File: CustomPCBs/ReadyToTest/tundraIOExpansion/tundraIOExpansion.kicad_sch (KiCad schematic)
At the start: 58 parts, among them J1 Conn_01x25, J2 Conn_ARM_SWD_TagConnect_TC203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, J3 Conn_ARM_SWD_TagConnect_TC203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, U1 RP2040, U2 W25Q32JVSS, U4 W25Q32JVSS, U5 RP2040, Y1 12.000MHz, Y2 12.000MHz, Y3 32.768kHz

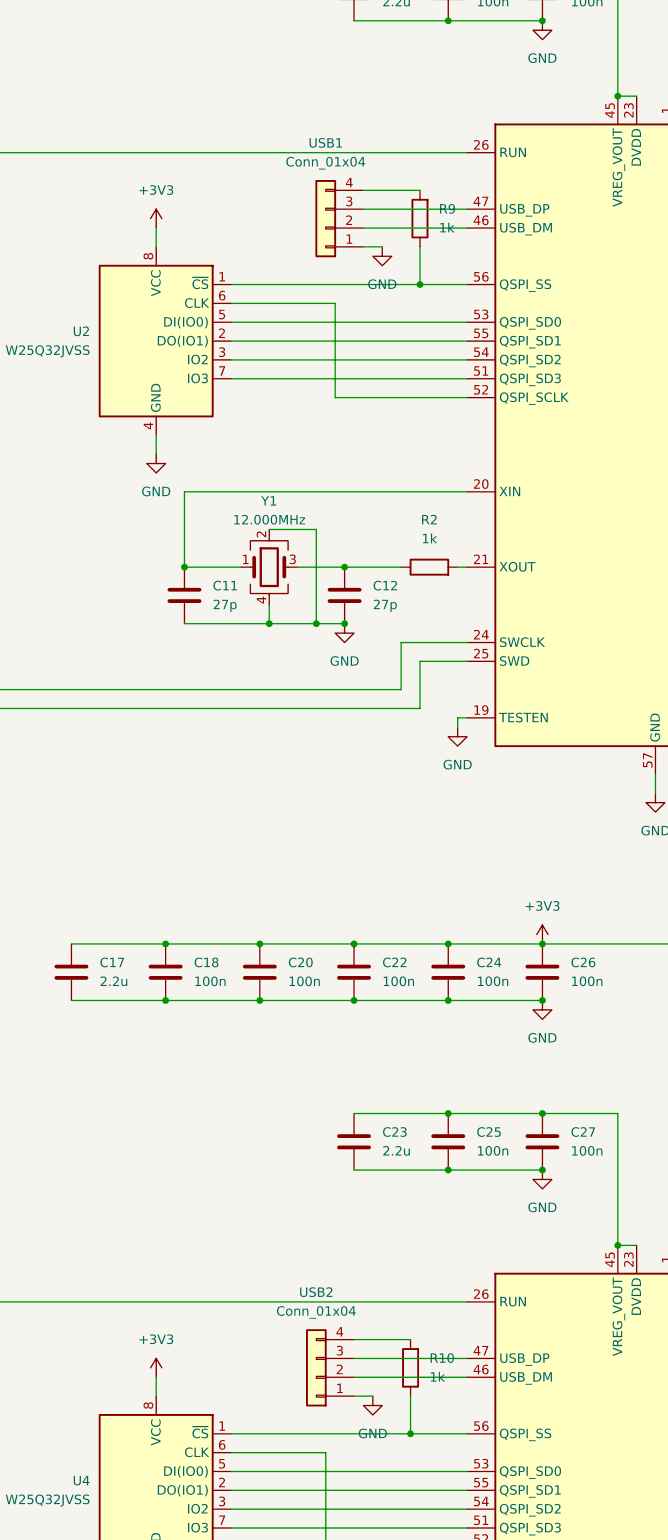
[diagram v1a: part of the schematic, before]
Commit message: Fixing USB connectors on main board
Forgot to invert the USB connectors, these were wrong too on the first
batch.
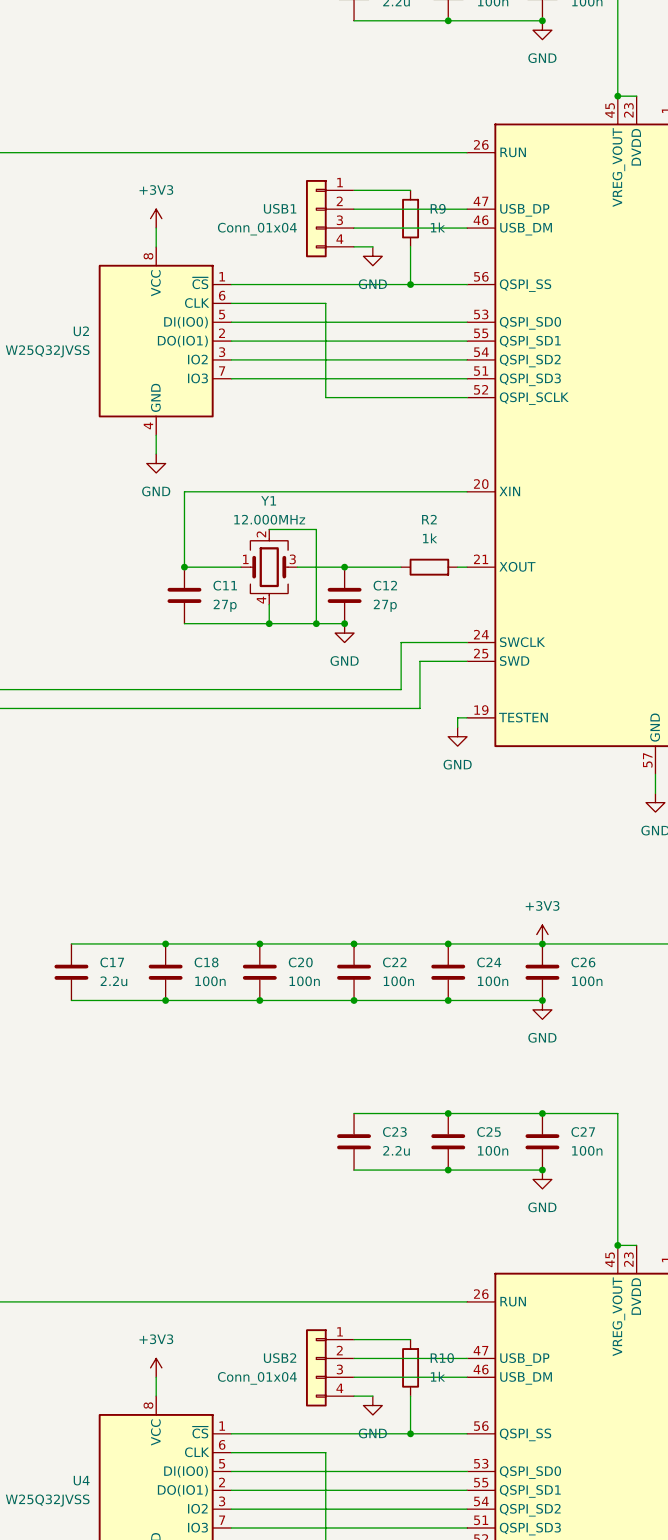
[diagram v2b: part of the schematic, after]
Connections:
- net GND: now also USB1.4 (Pin_4), USB2.4 (Pin_4); no longer USB1.1 (Pin_1), USB2.1 (Pin_1)
- net at U1.46 (USB_DM): now also USB1.3 (Pin_3); no longer USB1.2 (Pin_2)
- net at U1.47 (USB_DP): now also USB1.2 (Pin_2); no longer USB1.3 (Pin_3)
- net at R9.2: now also USB1.1 (Pin_1); no longer USB1.4 (Pin_4)
- net at R10.2: now also USB2.1 (Pin_1); no longer USB2.4 (Pin_4)
- net at USB2.2 (Pin_2): now also U5.47 (USB_DP); no longer U5.46 (USB_DM)
- net at USB2.3 (Pin_3): now also U5.46 (USB_DM); no longer U5.47 (USB_DP)
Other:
- moved on the sheet: R9, USB1, USB2
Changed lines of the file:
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@@
   (junction (at 189.23 198.12) (diameter 0) (color 0 0 0 0)
   )
-  (junction (at 139.7 86.36) (diameter 0) (color 0 0 0 0)
+  (junction (at 138.43 86.36) (diameter 0) (color 0 0 0 0)
   )
   (junction (at 279.4 248.92) (diameter 0) (color 0 0 0 0)
@@
     (stroke (width 0) (type default))
   )
-  (wire (pts (xy 132.08 73.66) (xy 139.7 73.66))
-    (stroke (width 0) (type default))
-  )
   (wire (pts (xy 363.22 243.84) (xy 363.22 254))
     (stroke (width 0) (type default))
@@
     (stroke (width 0) (type default))
   )
-  (wire (pts (xy 114.3 88.9) (xy 128.27 88.9))
+  (wire (pts (xy 114.3 88.9) (xy 127 88.9))
     (stroke (width 0) (type default))
   )
@@
     (stroke (width 0) (type default))
   )
+  (wire (pts (xy 130.81 78.74) (xy 146.05 78.74))
+    (stroke (width 0) (type default))
+  )
   (wire (pts (xy 143.51 50.8) (xy 156.21 50.8))
     (stroke (width 0) (type default))
@@
     (stroke (width 0) (type default))
   )
+  (wire (pts (xy 130.81 236.22) (xy 133.35 236.22))
+    (stroke (width 0) (type default))
+  )
   (wire (pts (xy 24.13 113.03) (xy 26.67 113.03))
     (stroke (width 0) (type default))
@@
     (stroke (width 0) (type default))
   )
-  (wire (pts (xy 128.27 101.6) (xy 146.05 101.6))
+  (wire (pts (xy 127 101.6) (xy 146.05 101.6))
     (stroke (width 0) (type default))
   )
@@
     (stroke (width 0) (type default))
   )
-  (wire (pts (xy 132.08 81.28) (xy 134.62 81.28))
+  (wire (pts (xy 24.13 120.65) (xy 26.67 120.65))
     (stroke (width 0) (type default))
   )
-  (wire (pts (xy 24.13 120.65) (xy 26.67 120.65))
+  (wire (pts (xy 130.81 231.14) (xy 146.05 231.14))
     (stroke (width 0) (type default))
   )
@@
     (stroke (width 0) (type default))
   )
+  (wire (pts (xy 130.81 228.6) (xy 138.43 228.6))
+    (stroke (width 0) (type default))
+  )
   (wire (pts (xy 143.51 20.32) (xy 130.81 20.32))
     (stroke (width 0) (type default))
   )
+  (wire (pts (xy 130.81 76.2) (xy 146.05 76.2))
+    (stroke (width 0) (type default))
+  )
   (wire (pts (xy 138.43 297.18) (xy 138.43 292.1))
     (stroke (width 0) (type default))
@@
     (stroke (width 0) (type default))
   )
+  (wire (pts (xy 130.81 73.66) (xy 138.43 73.66))
+    (stroke (width 0) (type default))
+  )
   (wire (pts (xy 196.85 101.6) (xy 203.2 101.6))
     (stroke (width 0) (type default))
@@
     (stroke (width 0) (type default))
   )
-  (wire (pts (xy 132.08 78.74) (xy 146.05 78.74))
-    (stroke (width 0) (type default))
-  )
   (wire (pts (xy 196.85 297.18) (xy 199.39 297.18))
     (stroke (width 0) (type default))
@@
     (stroke (width 0) (type default))
   )
+  (wire (pts (xy 130.81 233.68) (xy 146.05 233.68))
+    (stroke (width 0) (type default))
+  )
   (wire (pts (xy 279.4 294.64) (xy 279.4 297.18))
     (stroke (width 0) (type default))
@@
     (stroke (width 0) (type default))
   )
-  (wire (pts (xy 139.7 81.28) (xy 139.7 86.36))
+  (wire (pts (xy 138.43 81.28) (xy 138.43 86.36))
     (stroke (width 0) (type default))
   )
@@
     (stroke (width 0) (type default))
   )
-  (wire (pts (xy 130.81 236.22) (xy 133.35 236.22))
-    (stroke (width 0) (type default))
-  )
   (wire (pts (xy 262.89 68.58) (xy 259.08 68.58))
     (stroke (width 0) (type default))
@@
     (stroke (width 0) (type default))
   )
-  (wire (pts (xy 130.81 231.14) (xy 146.05 231.14))
-    (stroke (width 0) (type default))
-  )
   (wire (pts (xy 347.98 243.84) (xy 363.22 243.84))
     (stroke (width 0) (type default))
@@
     (stroke (width 0) (type default))
   )
-  (wire (pts (xy 130.81 233.68) (xy 146.05 233.68))
-    (stroke (width 0) (type default))
-  )
   (wire (pts (xy 279.4 297.18) (xy 279.4 298.45))
     (stroke (width 0) (type default))
   )
-  (wire (pts (xy 132.08 76.2) (xy 146.05 76.2))
-    (stroke (width 0) (type default))
-  )
   (wire (pts (xy 119.38 119.38) (xy 125.73 119.38))
     (stroke (width 0) (type default))
@@
     (stroke (width 0) (type default))
   )
-  (wire (pts (xy 139.7 86.36) (xy 146.05 86.36))
+  (wire (pts (xy 138.43 86.36) (xy 146.05 86.36))
     (stroke (width 0) (type default))
   )
@@
     (stroke (width 0) (type default))
   )
-  (wire (pts (xy 130.81 228.6) (xy 138.43 228.6))
-    (stroke (width 0) (type default))
-  )
   (wire (pts (xy 279.4 289.56) (xy 279.4 294.64))
     (stroke (width 0) (type default))
@@
     (stroke (width 0) (type default))
   )
-  (wire (pts (xy 128.27 88.9) (xy 128.27 101.6))
+  (wire (pts (xy 127 88.9) (xy 127 101.6))
+    (stroke (width 0) (type default))
+  )
+  (wire (pts (xy 130.81 81.28) (xy 133.35 81.28))
     (stroke (width 0) (type default))
   )
-  (wire (pts (xy 114.3 86.36) (xy 139.7 86.36))
+  (wire (pts (xy 114.3 86.36) (xy 138.43 86.36))
     (stroke (width 0) (type default))
   )
@@
     )
   )
-  (symbol (lib_id "power:GND") (at 134.62 81.28 0) (unit 1)
+  (symbol (lib_id "power:GND") (at 133.35 81.28 0) (unit 1)
     (in_bom yes) (on_board yes) (dnp no) (fields_autoplaced)
-    (property "Reference" "#PWR016" (at 134.62 87.63 0)
+    (property "Reference" "#PWR016" (at 133.35 87.63 0)
       (effects (font (size 1.27 1.27)) hide)
     )
-    (property "Value" "GND" (at 134.62 86.36 0)
+    (property "Value" "GND" (at 133.35 86.36 0)
       (effects (font (size 1.27 1.27)))
     )
-    (property "Footprint" "" (at 134.62 81.28 0)
+    (property "Footprint" "" (at 133.35 81.28 0)
       (effects (font (size 1.27 1.27)) hide)
     )
-    (property "Datasheet" "" (at 134.62 81.28 0)
+    (property "Datasheet" "" (at 133.35 81.28 0)
       (effects (font (size 1.27 1.27)) hide)
     )
@@
     )
   )
-  (symbol (lib_id "Device:R") (at 139.7 77.47 180) (unit 1)
+  (symbol (lib_id "Device:R") (at 138.43 77.47 180) (unit 1)
     (in_bom yes) (on_board yes) (dnp no) (fields_autoplaced)
-    (property "Reference" "R9" (at 142.24 76.2 0)
+    (property "Reference" "R9" (at 140.97 76.2 0)
       (effects (font (size 1.27 1.27)) (justify right))
     )
-    (property "Value" "1k" (at 142.24 78.74 0)
+    (property "Value" "1k" (at 140.97 78.74 0)
       (effects (font (size 1.27 1.27)) (justify right))
     )
-    (property "Footprint" "Resistor_SMD:R_0402_1005Metric" (at 141.478 77.47 90)
+    (property "Footprint" "Resistor_SMD:R_0402_1005Metric" (at 140.208 77.47 90)
       (effects (font (size 1.27 1.27)) hide)
     )
-    (property "Datasheet" "~" (at 139.7 77.47 0)
+    (property "Datasheet" "~" (at 138.43 77.47 0)
       (effects (font (size 1.27 1.27)) hide)
     )
@@
     )
   )
-  (symbol (lib_id "Connector_Generic:Conn_01x04") (at 127 78.74 180) (unit 1)
-    (in_bom yes) (on_board yes) (dnp no) (fields_autoplaced)
-    (property "Reference" "USB1" (at 127 67.31 0)
-      (effects (font (size 1.27 1.27)))
+  (symbol (lib_id "Connector_Generic:Conn_01x04") (at 125.73 76.2 0) (mirror y) (unit 1)
+    (in_bom yes) (on_board yes) (dnp no)
+    (property "Reference" "USB1" (at 123.19 76.2 0)
+      (effects (font (size 1.27 1.27)) (justify left))
     )
-    (property "Value" "Conn_01x04" (at 127 69.85 0)
-      (effects (font (size 1.27 1.27)))
+    (property "Value" "Conn_01x04" (at 123.19 78.74 0)
+      (effects (font (size 1.27 1.27)) (justify left))
     )
-    (property "Footprint" "Connector_JST:JST_SH_SM04B-SRSS-TB_1x04-1MP_P1.00mm_Horizontal" (at 127 78.74 0)
+    (property "Footprint" "Connector_JST:JST_SH_SM04B-SRSS-TB_1x04-1MP_P1.00mm_Horizontal" (at 125.73 76.2 0)
       (effects (font (size 1.27 1.27)) hide)
     )
-    (property "Datasheet" "~" (at 127 78.74 0)
+    (property "Datasheet" "~" (at 125.73 76.2 0)
       (effects (font (size 1.27 1.27)) hide)
     )
@@
     )
   )
-  (symbol (lib_id "Connector_Generic:Conn_01x04") (at 125.73 233.68 180) (unit 1)
-    (in_bom yes) (on_board yes) (dnp no) (fields_autoplaced)
-    (property "Reference" "USB2" (at 125.73 222.25 0)
-      (effects (font (size 1.27 1.27)))
+  (symbol (lib_id "Connector_Generic:Conn_01x04") (at 125.73 231.14 0) (mirror y) (unit 1)
+    (in_bom yes) (on_board yes) (dnp no)
+    (property "Reference" "USB2" (at 123.19 231.14 0)
+      (effects (font (size 1.27 1.27)) (justify left))
     )
-    (property "Value" "Conn_01x04" (at 125.73 224.79 0)
-      (effects (font (size 1.27 1.27)))
+    (property "Value" "Conn_01x04" (at 123.19 233.68 0)
+      (effects (font (size 1.27 1.27)) (justify left))
     )
-    (property "Footprint" "Connector_JST:JST_SH_SM04B-SRSS-TB_1x04-1MP_P1.00mm_Horizontal" (at 125.73 233.68 0)
+    (property "Footprint" "Connector_JST:JST_SH_SM04B-SRSS-TB_1x04-1MP_P1.00mm_Horizontal" (at 125.73 231.14 0)
       (effects (font (size 1.27 1.27)) hide)
     )
-    (property "Datasheet" "~" (at 125.73 233.68 0)
+    (property "Datasheet" "~" (at 125.73 231.14 0)
       (effects (font (size 1.27 1.27)) hide)
     )
